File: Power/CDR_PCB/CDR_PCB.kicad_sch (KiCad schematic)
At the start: 59 parts, among them IC1 TEENSY_4.1, J1 +5V, J10 Transceiver header, J2 +3V3, J3 Lower_PCB_Header, J4 +28V, J5 +14Vin, J6 +14Vout, J7 MOTOR2, J8 MOTOR1, J9 Converter_GND_Lines, U1 INA226, U2 BNO055, U3 DPS310XTSA1, U4 GNSS, U5 DRV8871, U6 MICROFC-30035-SMT-TR1, U7 HTS221, U8 OPA333xxD, U9 OPA333xxD

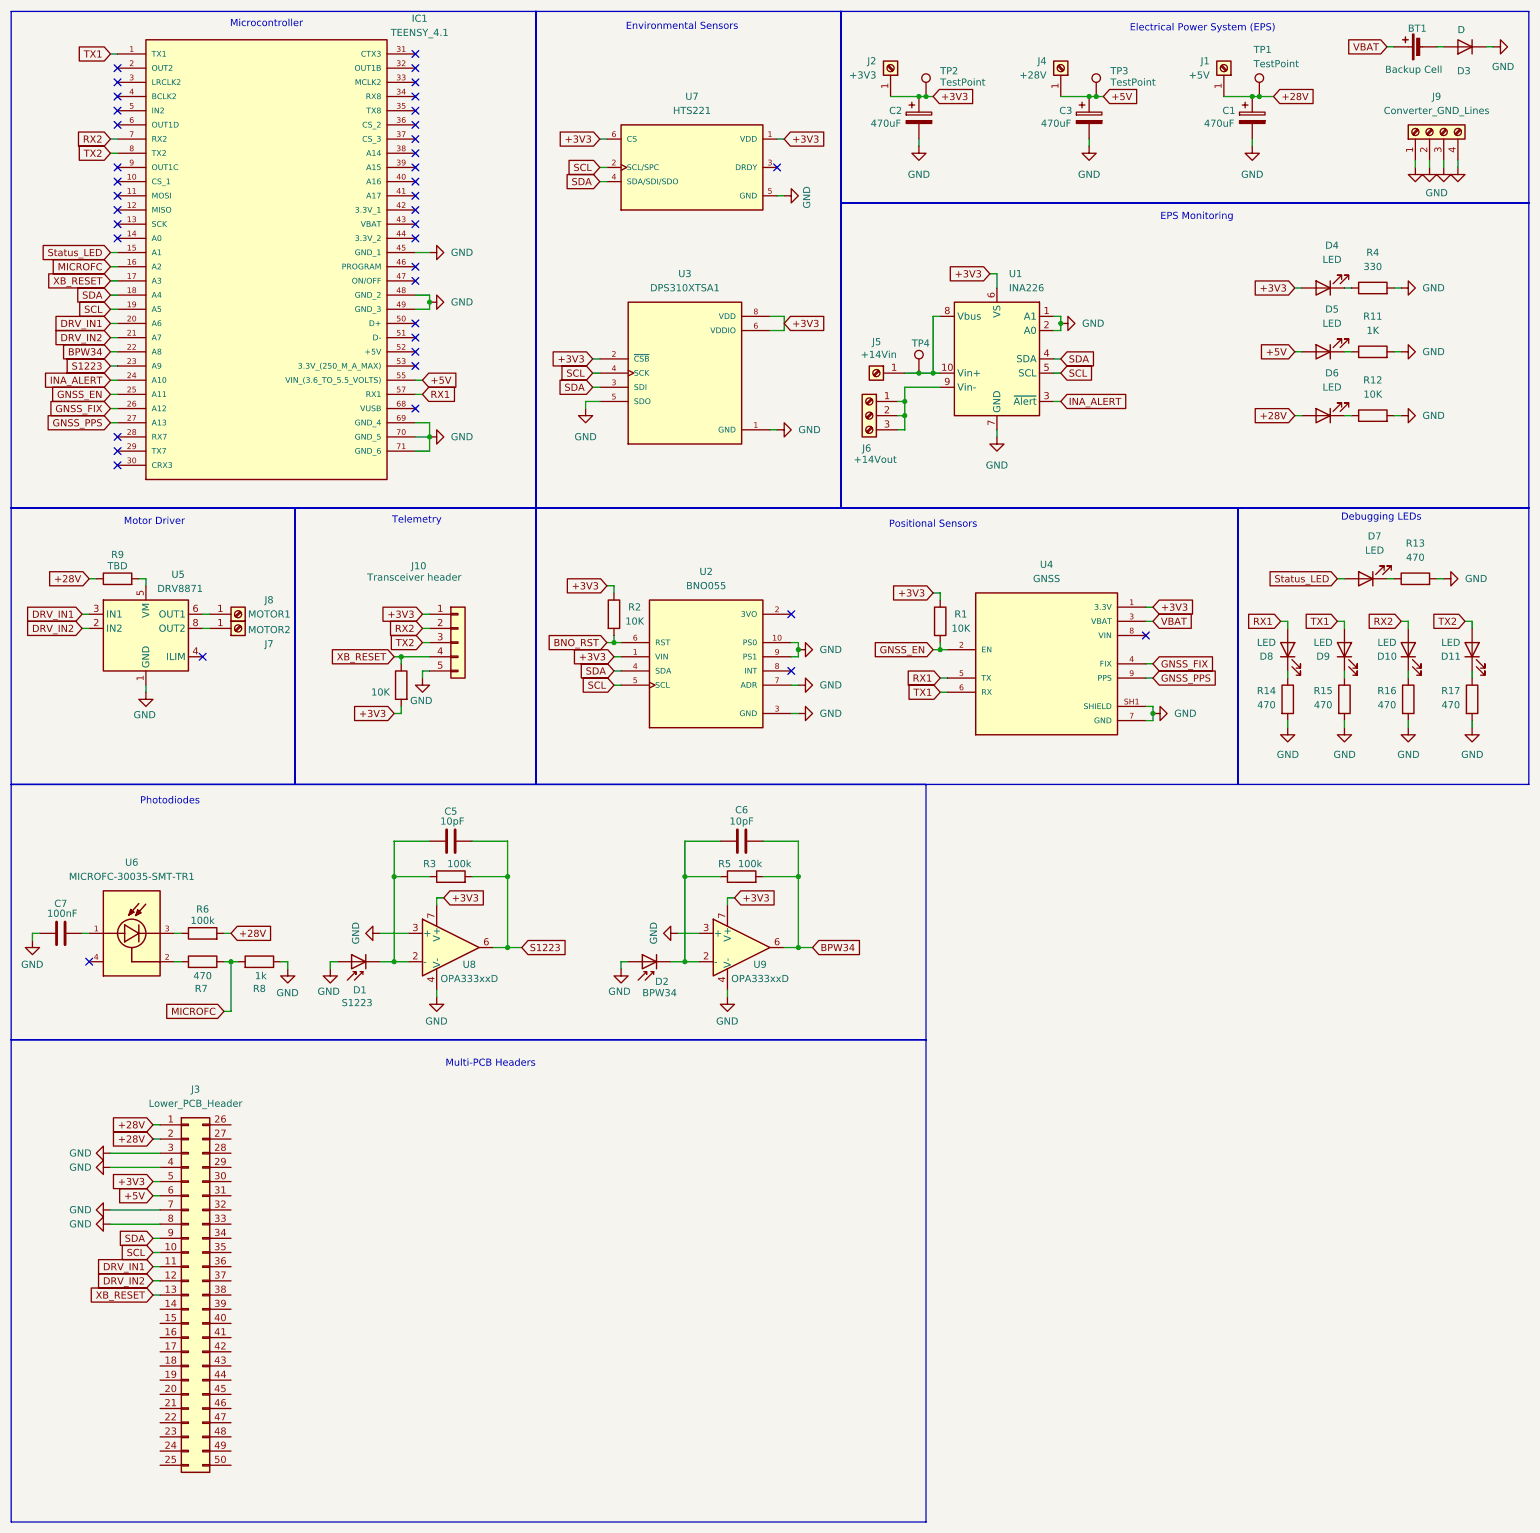
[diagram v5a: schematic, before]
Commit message: Adjusted EPS for CCA
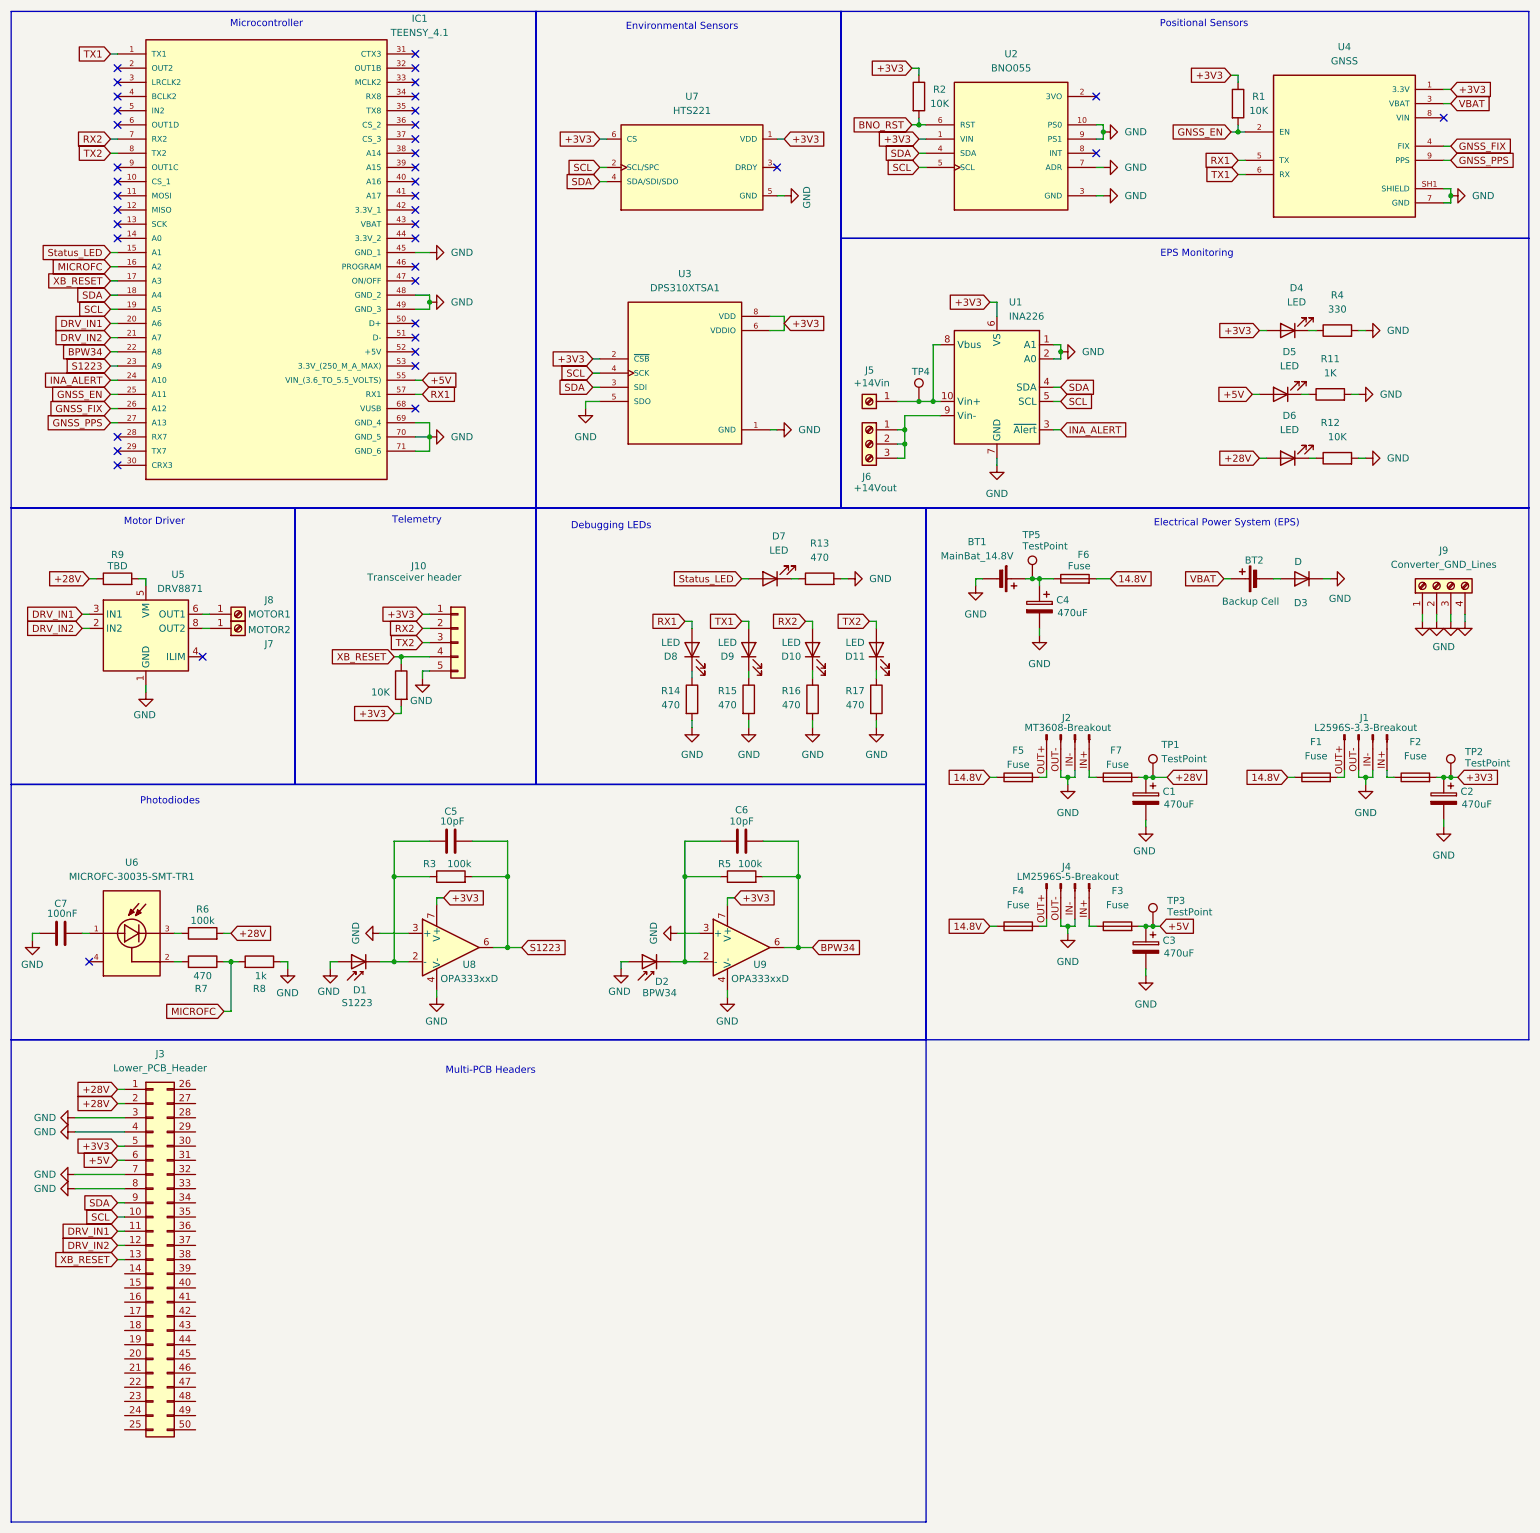
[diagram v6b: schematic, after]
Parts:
- removed J1: +5V, Connector_PinHeader_2.54mm:PinHeader_1x01_P2.54mm_Vertical, symbol Connector:Screw_Terminal_01x01
- removed J2: +3V3, Connector_PinHeader_2.54mm:PinHeader_1x01_P2.54mm_Vertical, symbol Connector:Screw_Terminal_01x01
- removed J4: +28V, Connector_PinHeader_2.54mm:PinHeader_1x01_P2.54mm_Vertical, symbol Connector:Screw_Terminal_01x01
- added BT1: MainBat_14.8V, symbol Device:Battery_Cell
- added C4: 470uF, Capacitor_THT:CP_Radial_D8.0mm_P3.50mm, symbol Device:C_Polarized
- added F1, F2, F3, F4, F5, F6, F7: Fuse, symbol Device:Fuse
- added J1: L2596S-3.3-Breakout, symbol Connector:Conn_01x04_Pin
- added J2: MT3608-Breakout, symbol Connector:Conn_01x04_Pin
- added J4: LM2596S-5-Breakout, symbol Connector:Conn_01x04_Pin
- added TP5: TestPoint, TestPoint:TestPoint_Loop_D2.50mm_Drill1.0mm, symbol Connector:TestPoint
- renumbered BT1 to BT2
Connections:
- net +28V: now also F7.2
- net +3V3: now also F2.2
- net +5V: now also F3.2
- net GND: now also BT1.2 (-), C4.2, J1.IN- (Pin_2), J1.OUT- (Pin_3), J2.IN- (Pin_2), J2.OUT- (Pin_3), J4.IN- (Pin_2), J4.OUT- (Pin_3)
- new net: F7.1, J2.IN+ (Pin_1)
- new net: F5.2, J2.OUT+ (Pin_4)
- new net: F1.2, J1.OUT+ (Pin_4)
- new net: BT1.1 (+), C4.1, F6.1, TP5.1
- new net: F2.1, J1.IN+ (Pin_1)
- new net: F3.1, J4.IN+ (Pin_1)
- new net: F4.2, J4.OUT+ (Pin_4)
- new net 14.8V: F1.1, F4.1, F5.1, F6.2
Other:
- moved on the sheet: BT2, C1, C2, C3, D10, D11, D3, D4, D5, D6, D7, D8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
